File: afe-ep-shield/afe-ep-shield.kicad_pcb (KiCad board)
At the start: 2 copper layers, 65 x 60 mm, 35 parts, among them J1 Conn_02x06_Odd_Even, J2 Conn_02x06_Odd_Even, J3 Conn_02x12_Odd_Even, J4 Conn_02x12_Odd_Even, J5 Conn_02x20_Odd_Even, U1 Dual_Buffer, U2 Dual_Buffer, U3 HFBR-2521Z, U4 HFBR-1521Z, U5 HFBR-1521Z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

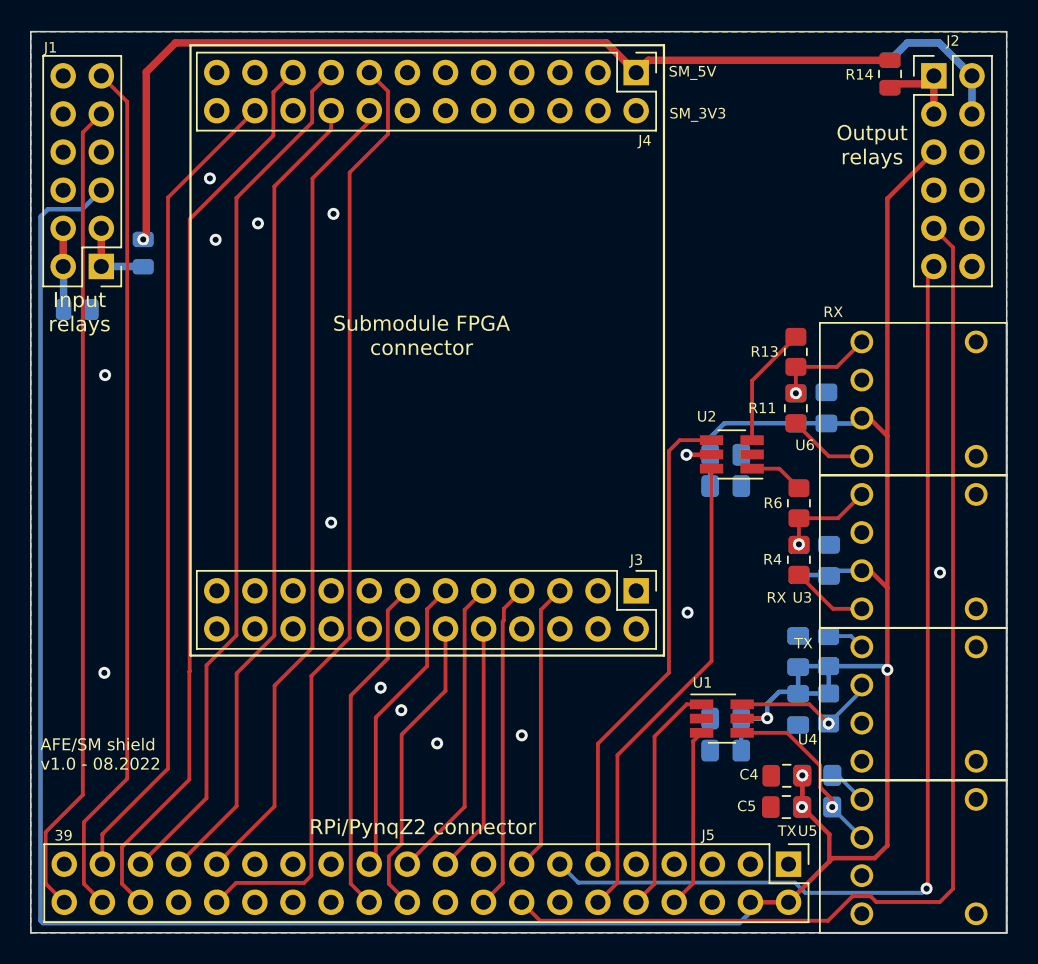
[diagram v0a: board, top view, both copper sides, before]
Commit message: Fixed afe shield connector
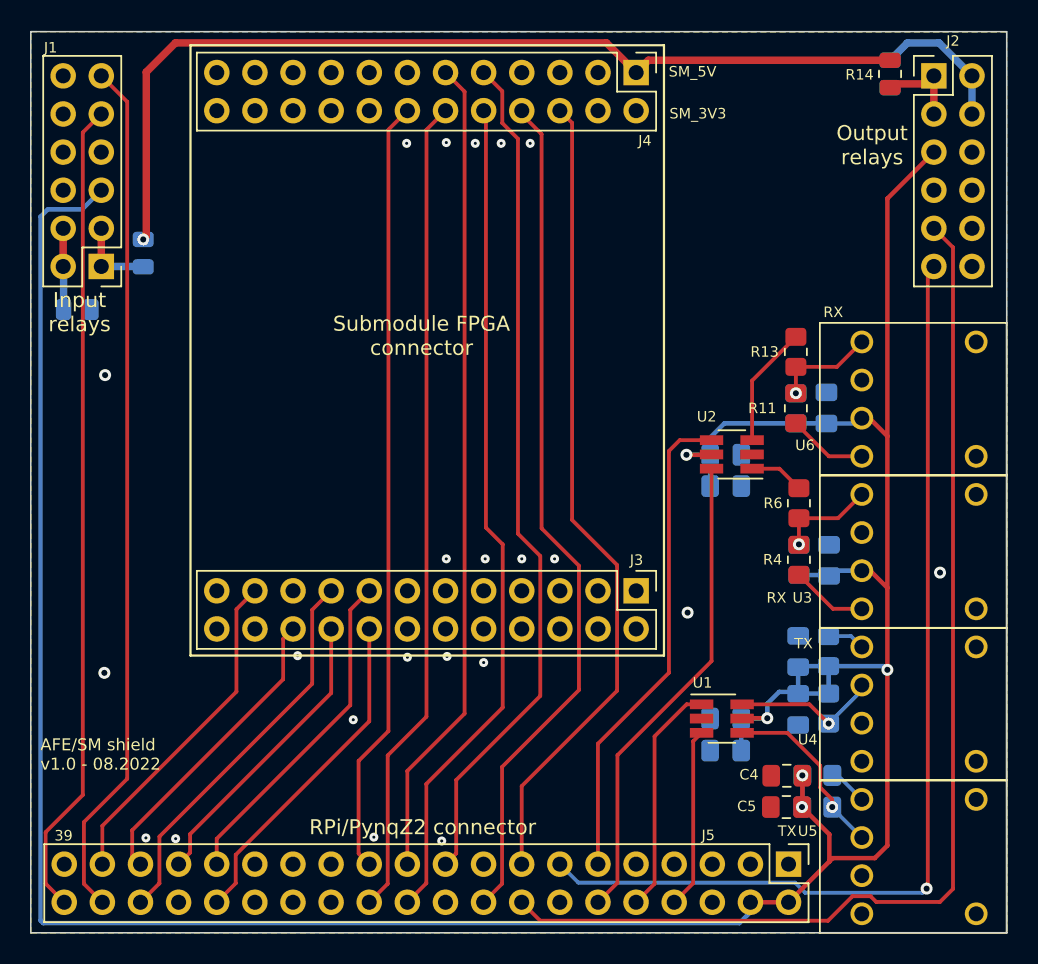
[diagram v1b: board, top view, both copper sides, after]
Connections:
- net /EXT_CLK renamed /RPIO_14
- net /EXT_SD1 renamed /RPIO_18
- net /EXT_SD2 renamed /RPIO_17
- net /EXT_~CS renamed /RPIO_15
- net /RL1_in renamed /RPIO_20
- net /RL1_out renamed /RPIO_27
- net /RL2_in renamed /RPIO_21
- net /RL2_out renamed /RPIO_23
- J3 pad 10: /RPIO_10 -> unconnected-(J3-Pad10)
- J3 pad 11: /RPIO_11 -> unconnected-(J3-Pad11)
- J3 pad 12: /RPIO_25 -> unconnected-(J3-Pad12)
- J3 pad 13: /RPIO_08 -> unconnected-(J3-Pad13)
- J3 pad 15: unconnected-(J3-Pad15) -> /I1_~CS
- J3 pad 16: unconnected-(J3-Pad16) -> /I1_SD
- J3 pad 17: unconnected-(J3-Pad17) -> /I1_CLK
- J3 pad 18: unconnected-(J3-Pad18) -> /RPIO_13
- J3 pad 20: unconnected-(J3-Pad20) -> /V1_CLK
- J3 pad 21: unconnected-(J3-Pad21) -> /RPIO_26
- J3 pad 5: /RPIO_22 -> unconnected-(J3-Pad5)
- J3 pad 7: /RPIO_24 -> unconnected-(J3-Pad7)
- J3 pad 9: /RPIO_09 -> unconnected-(J3-Pad9)
- J4 pad 10: unconnected-(J4-Pad10) -> /RPIO_25
- J4 pad 11: unconnected-(J4-Pad11) -> /RPIO_09
- J4 pad 12: unconnected-(J4-Pad12) -> /RPIO_08
- J4 pad 14: unconnected-(J4-Pad14) -> /RPIO_11
- J4 pad 15: /I1_SD -> unconnected-(J4-Pad15)
- J4 pad 16: /I1_~CS -> unconnected-(J4-Pad16)
- J4 pad 17: /RPIO_19 -> unconnected-(J4-Pad17)
- J4 pad 18: /I1_CLK -> unconnected-(J4-Pad18)
- J4 pad 19: /RPIO_16 -> unconnected-(J4-Pad19)
- J4 pad 22: /RPIO_26 -> unconnected-(J4-Pad22)
- J4 pad 6: unconnected-(J4-Pad6) -> /RPIO_22
- J4 pad 8: unconnected-(J4-Pad8) -> /RPIO_24
- J4 pad 9: unconnected-(J4-Pad9) -> /RPIO_10
- J5 pad 33: /I1_CLK -> /RPIO_13
- J5 pad 35: /RPIO_19 -> /V1_CLK
- J5 pad 36: /RPIO_16 -> /I1_CLK
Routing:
- net /RPIO_16: track 60.5 -> 0.00 mm
- net /RPIO_19: track 58.0 -> 0.00 mm
- net /I1_SD: track 63.2 -> 22.4 mm
- net /RPIO_10: track 16.7 -> 56.9 mm
- net /RPIO_25: track 20.3 -> 55.9 mm
- net /RPIO_24: track 21.8 -> 57.0 mm
- net /RPIO_22: track 19.3 -> 54.4 mm
- net /RPIO_09: track 20.3 -> 54.8 mm
- net /RPIO_08: track 22.8 -> 54.8 mm
- net /I1_~CS: track 54.4 -> 22.4 mm
- net /RPIO_26: track 54.4 -> 22.4 mm
- net /RPIO_11: track 20.3 -> 51.8 mm
- net /I1_CLK: track 54.4 -> 26.0 mm
- net /V1_CLK: track 0.00 -> 20.3 mm
- net /RPIO_13: track 0.00 -> 19.9 mm
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
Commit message: Connected 3V3A and 3V3 in afe shield
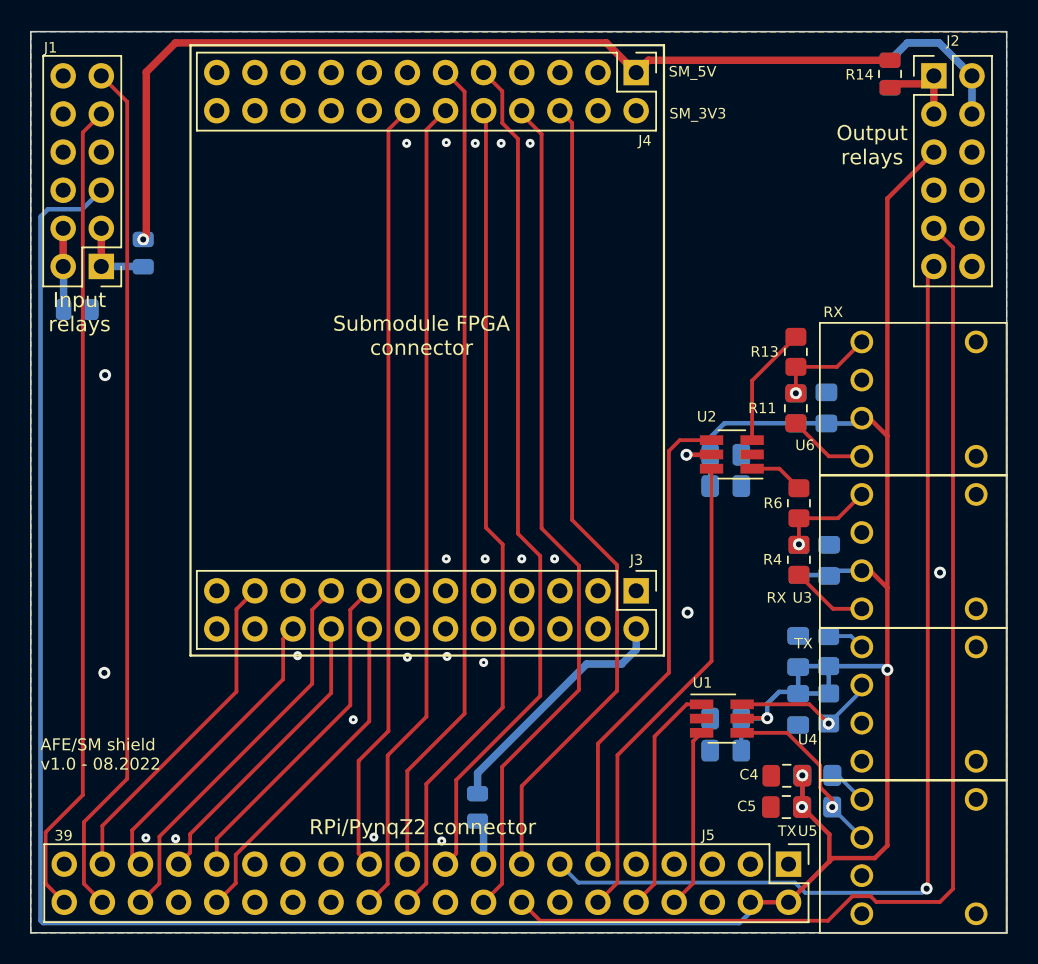
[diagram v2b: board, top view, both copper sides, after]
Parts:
- added R3: 0R, Resistor_SMD:R_0805_2012Metric, B.Cu at (89.7, 70.2)
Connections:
- net /RPIO_14 renamed /EXT_CLK
- net /RPIO_15 renamed /EXT_~CS
- net /RPIO_17 renamed /EXT_SD2
- net /RPIO_18 renamed /EXT_SD1
- net /RPIO_20 renamed /RL1_in
- net /RPIO_21 renamed /RL2_in
- net /RPIO_23 renamed /RL2_out
- net /RPIO_27 renamed /RL1_out
- net /V1_CLK renamed /RPIO_19
- J3 pad 2: unconnected-(J3-Pad2) -> +3V3A
- J4 pad 2: +3V3A -> unconnected-(J4-Pad2)
- J5 pad 1: +3V3 -> unconnected-(J5-Pad1)
- J5 pad 17: GND -> +3V3
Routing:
- net +3V3A: track 0.00 -> 16.7 mm
- net +3V3: track 0.00 -> 3.04 mm

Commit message: Corrected relay connector and generated gerber files for afe shield
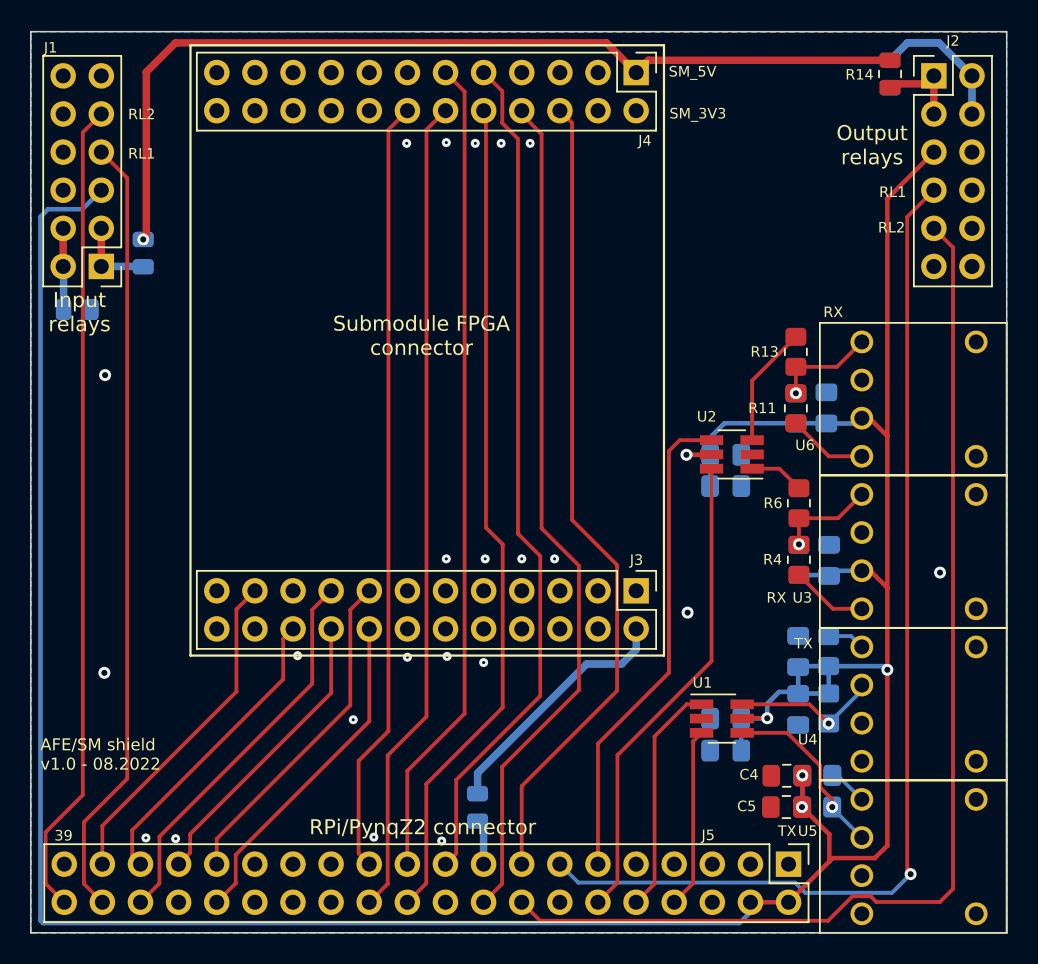
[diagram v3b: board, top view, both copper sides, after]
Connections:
- J1 pad 11: /RL1_in -> unconnected-(J1-Pad11)
- J1 pad 7: unconnected-(J1-Pad7) -> /RL1_in
- J2 pad 11: /RL1_out -> unconnected-(J2-Pad11)
- J2 pad 7: unconnected-(J2-Pad7) -> /RL1_out
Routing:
- net /RL1_in: track 57.5 -> 52.4 mm
- net /RL1_out: track 67.0 -> 71.1 mm
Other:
- board text added: "RL1"
- board text added: "RL2"
